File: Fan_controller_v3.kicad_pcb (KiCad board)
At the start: 4 copper layers, 50 x 25 mm, 0 parts

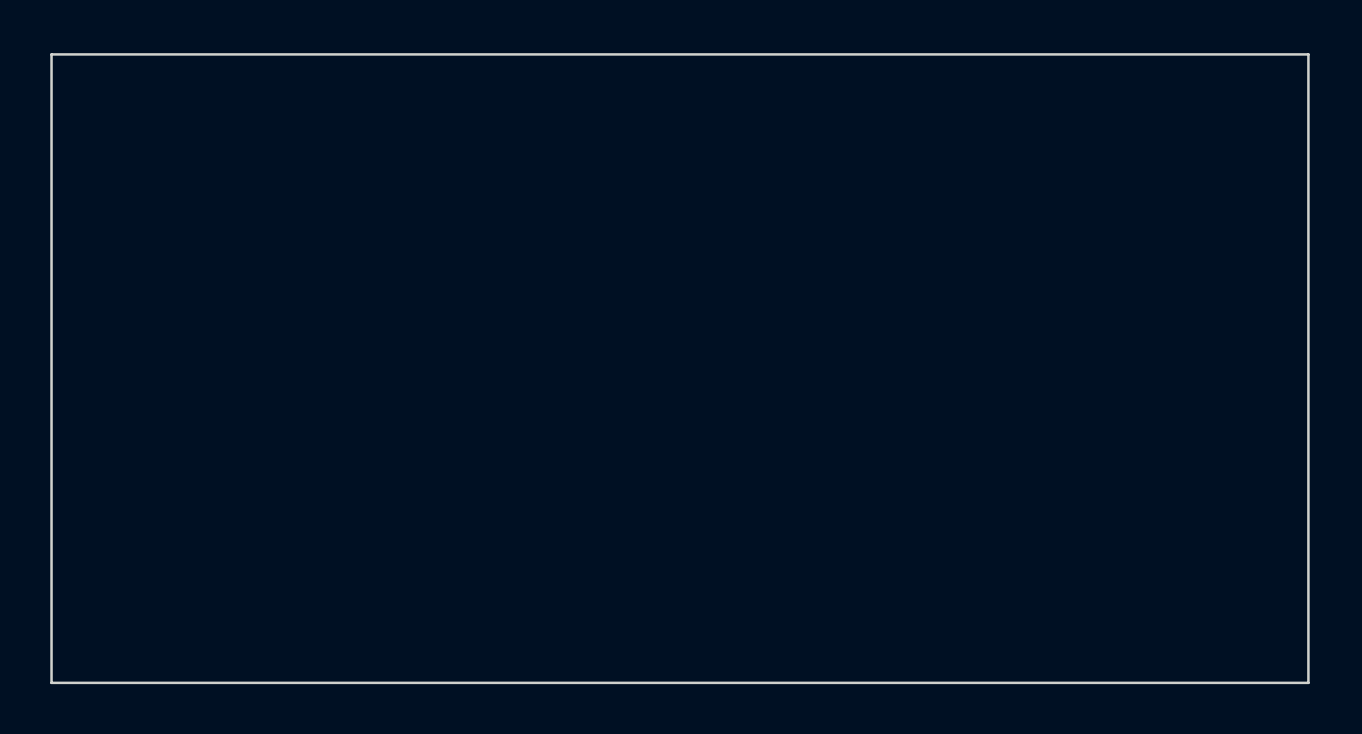
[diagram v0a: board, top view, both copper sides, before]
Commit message: Исправления в схеме и в печатной плате. Смещен вверх боковой конденсатор.
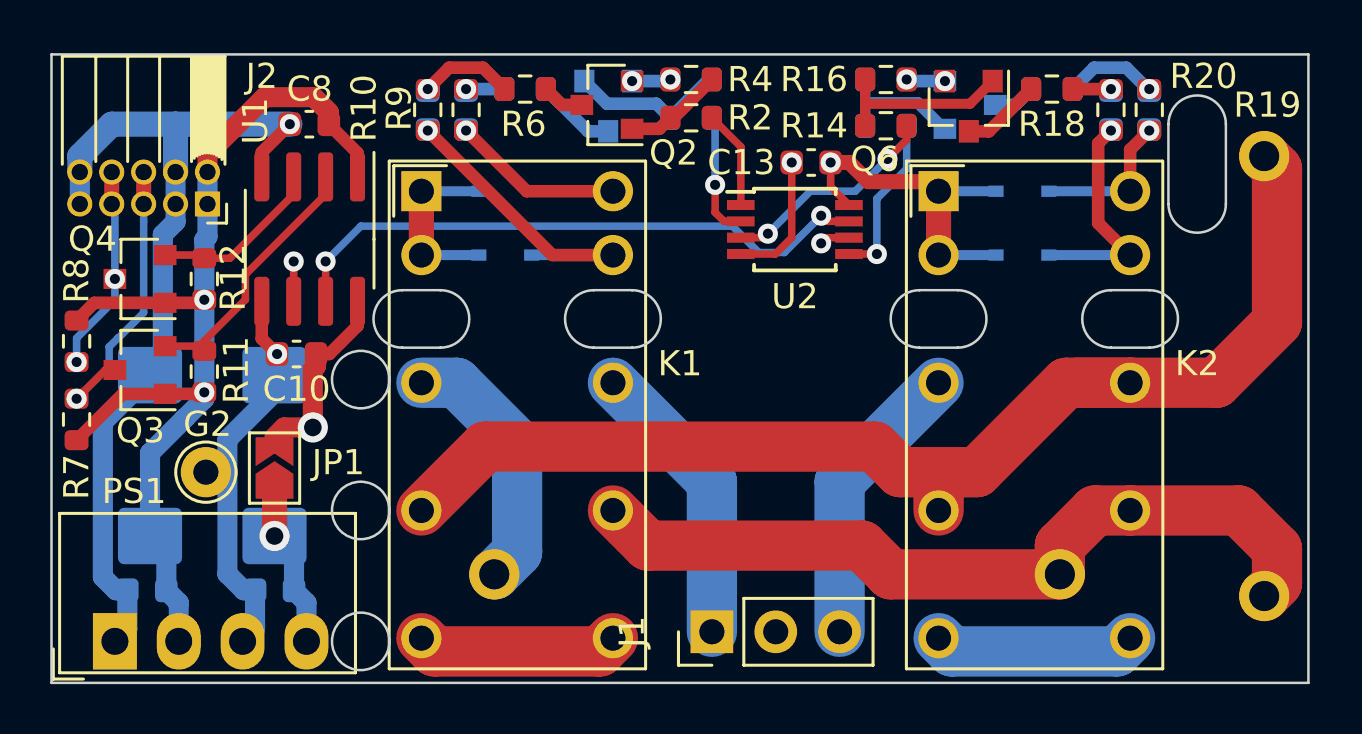
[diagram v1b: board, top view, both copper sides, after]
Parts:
- added C1: 10uF, Capacitor_Tantalum_SMD:CP_EIA-7343-43_Kemet-X_Pad2.25x2.55mm_HandSolder, B.Cu at (78.9, 91.0)
- added C10: 100nF, Capacitor_SMD:C_0603_1608Metric, F.Cu at (84.7, 86.9)
- added C11: 10uF, Capacitor_SMD:C_0603_1608Metric, B.Cu at (118.7, 77.2)
- added C12: 10uF, Capacitor_SMD:C_0603_1608Metric, B.Cu at (117.1, 77.2)
- added C13: 100nF, Capacitor_SMD:C_0603_1608Metric, F.Cu at (105.2, 79.3)
- added C2: 100nF, Capacitor_SMD:C_0603_1608Metric, B.Cu at (78.8, 96.3)
- added C3: 10uF, Capacitor_SMD:C_0603_1608Metric, B.Cu at (91.5, 77.2)
- added C4: 10uF, Capacitor_SMD:C_0603_1608Metric, B.Cu at (90.0, 77.2)
- added C5: 0.47uF, Modules:C_K73-17_W26.0mm_H15.0mm_T9.0mm_P22.5mm_d0.8mm_Horiz2, B.Cu at (92.6, 95.7)
- added C6: 100nF, Capacitor_SMD:C_0603_1608Metric, B.Cu at (83.9, 96.3)
- added C7: 0.22uF, Modules:C_K73-17_W20.0mm_H14.5mm_T8.0mm_P17.5mm_d0.8mm, B.Cu at (123.2, 79.0)
- added C8: 100nF, Capacitor_SMD:C_0603_1608Metric, F.Cu at (85.3, 77.8)
- added C9: 100uF, Capacitor_Tantalum_SMD:CP_EIA-7343-43_Kemet-X_Pad2.25x2.55mm_HandSolder, B.Cu at (83.9, 91.0)
- added D1: 1N4148WS, Diode_SMD:D_SOD-323, B.Cu at (93.0, 80.4)
- added D2: 1N4148WS, Diode_SMD:D_SOD-323, B.Cu at (93.0, 83.0)
- added D3: 1N4148WS, Diode_SMD:D_SOD-323, B.Cu at (113.6, 80.4)
- added D4: 1N4148WS, Diode_SMD:D_SOD-323, B.Cu at (113.6, 83.0)
- added G2: GND, TestPoint:TestPoint_THTPad_D2.0mm_Drill1.0mm, F.Cu at (81.1, 91.6)
- added J1: Load2, Modules:PinHeader_1x03_P2.54mm, F.Cu at (101.3, 98.0)
- added J2: Dig_mod_iface, Connector_PinSocket_1.27mm:PinSocket_2x05_P1.27mm_Horizontal, F.Cu at (81.2, 81.0)
- added JP1: 5P_en, Jumper:SolderJumper-2_P1.3mm_Open_TrianglePad1.0x1.5mm, F.Cu at (83.9, 91.5)
- added K1: HFD2_005-S-L2-D_Split, Modules:HFD2-005-S-L2-D, F.Cu at (89.7, 80.4)
- added K2: HFD2_005-S-L2-D_Split, Modules:HFD2-005-S-L2-D, F.Cu at (110.3, 80.4)
- added PS1: B0505S, Modules:B0505S, F.Cu at (77.5, 98.3)
- added Q1: 2N5551S, Package_TO_SOT_SMD:SOT-23, B.Cu at (97.1, 77.1)
- added Q2: 2N5551S, Package_TO_SOT_SMD:SOT-23, F.Cu at (97.1, 77.0)
- added Q3: BSS138, Package_TO_SOT_SMD:SOT-23, F.Cu at (78.5, 87.6)
- added Q4: BSS138, Package_TO_SOT_SMD:SOT-23, F.Cu at (78.5, 83.9)
- added Q5: 2N5551S, Package_TO_SOT_SMD:SOT-23, B.Cu at (111.5, 77.0)
- added Q6: 2N5551S, Package_TO_SOT_SMD:SOT-23, F.Cu at (111.5, 77.1)
- added R1: 1k, Resistor_SMD:R_0603_1608Metric, B.Cu at (100.4, 77.5)
- added R10: 820, Resistor_SMD:R_0603_1608Metric, F.Cu at (90.0, 77.2)
- added R11: 10k, Resistor_SMD:R_0603_1608Metric, F.Cu at (81.1, 87.6)
- added R12: 10k, Resistor_SMD:R_0603_1608Metric, F.Cu at (81.1, 83.9)
- added R13: 1k, Resistor_SMD:R_0603_1608Metric, B.Cu at (108.2, 77.8)
- added R14: 1k, Resistor_SMD:R_0603_1608Metric, F.Cu at (108.2, 77.8)
- added R15: 20k, Resistor_SMD:R_0603_1608Metric, B.Cu at (108.2, 76.0)
- added R16: 20k, Resistor_SMD:R_0603_1608Metric, F.Cu at (108.2, 76.0)
- added R17: 47, Resistor_SMD:R_0603_1608Metric, B.Cu at (114.8, 76.4)
- added R18: 47, Resistor_SMD:R_0603_1608Metric, F.Cu at (114.8, 76.4)
- added R19: 820, Resistor_SMD:R_0603_1608Metric, F.Cu at (118.7, 77.2)
- added R2: 1k, Resistor_SMD:R_0603_1608Metric, F.Cu at (100.4, 77.5)
- added R20: 820, Resistor_SMD:R_0603_1608Metric, F.Cu at (117.1, 77.2)
- added R3: 20k, Resistor_SMD:R_0603_1608Metric, B.Cu at (100.4, 76.0)
- added R4: 20k, Resistor_SMD:R_0603_1608Metric, F.Cu at (100.4, 76.0)
- added R5: 47, Resistor_SMD:R_0603_1608Metric, B.Cu at (93.8, 76.4)
- added R6: 47, Resistor_SMD:R_0603_1608Metric, F.Cu at (93.8, 76.4)
- added R7: 10G, Resistor_SMD:R_0603_1608Metric, F.Cu at (76.0, 89.5)
- added R8: 10G, Resistor_SMD:R_0603_1608Metric, F.Cu at (76.0, 86.4)
- added R9: 820, Resistor_SMD:R_0603_1608Metric, F.Cu at (91.5, 77.2)
- added U1: ADuM1251ARZ, Package_SO:SOIC-8_3.9x4.9mm_P1.27mm, F.Cu at (85.3, 82.3)
- added U2: PCA9536DP, Package_SO:TSSOP-8_3x3mm_P0.65mm, F.Cu at (104.6, 82.0)
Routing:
- net Net-(C7-Pad1): track 0.00 -> 48.6 mm
- net +5P: track 0.00 -> 41.2 mm, vias 0 -> 2
- net GND1: track 0.00 -> 36.0 mm, vias 0 -> 1
- net Net-(C5-Pad2): track 0.00 -> 31.9 mm
- net +5VP: track 0.00 -> 29.2 mm, vias 0 -> 2
- net /I2C_SCL: track 0.00 -> 24.9 mm, vias 0 -> 2
- net GND2: track 0.00 -> 24.8 mm, vias 0 -> 6
- net /I2C_SDA: track 0.00 -> 24.1 mm, vias 0 -> 2
- net Net-(C4-Pad2): track 0.00 -> 12.7 mm, vias 0 -> 1
- net /sda0: track 0.00 -> 12.1 mm, vias 0 -> 1
- net Net-(J1-Pad3): track 0.00 -> 11.5 mm
- net Net-(J1-Pad1): track 0.00 -> 11.5 mm
- net Net-(Q5-Pad1): track 0.00 -> 10.9 mm
- net Net-(Q3-Pad2): track 0.00 -> 10.6 mm
- net Net-(C5-Pad1): track 0.00 -> 10.4 mm
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- added copper zone on In1.Cu, net +5VP
- added copper zone on In2.Cu, net GND2
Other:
- outline, holes or cut-outs redrawn

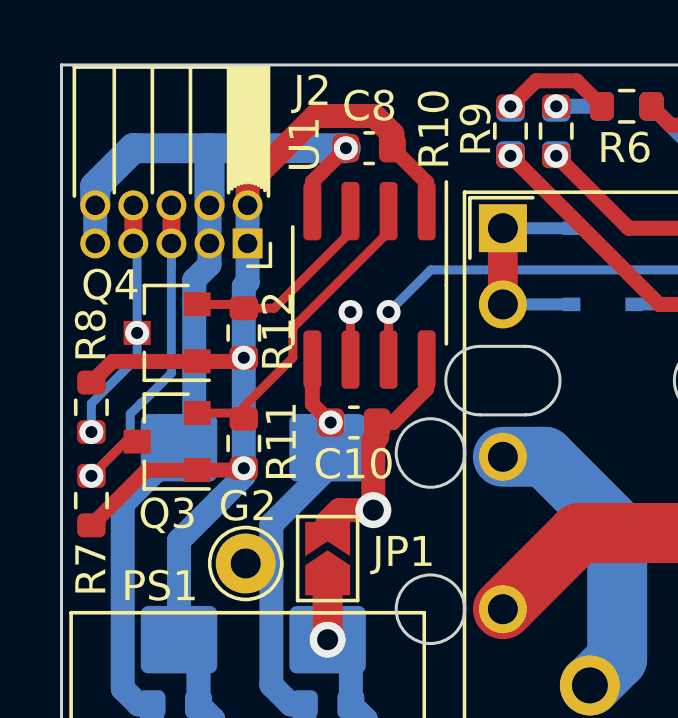
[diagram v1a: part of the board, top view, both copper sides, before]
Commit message: Добавлены недостающие компоненты схемы. Закончена трассировка платы.
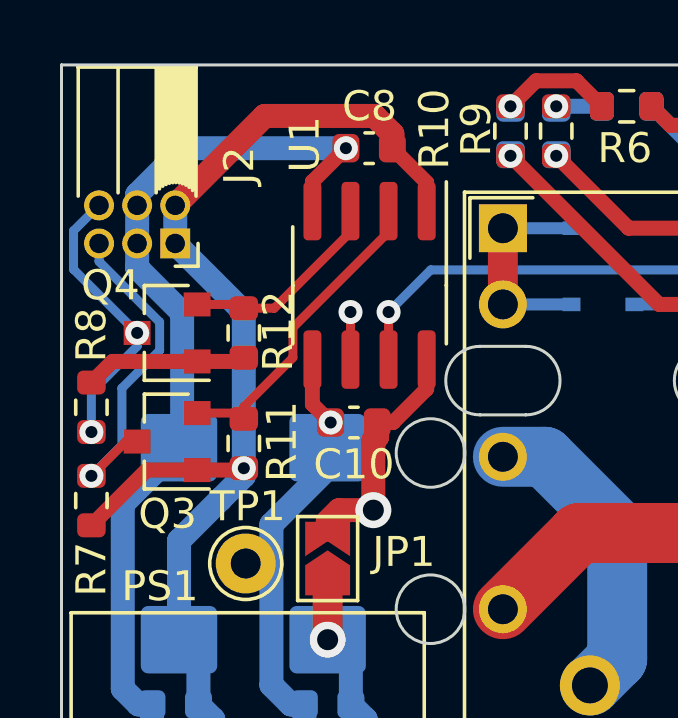
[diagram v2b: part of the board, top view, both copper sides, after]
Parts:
- J2: footprint Connector_PinSocket_1.27mm:PinSocket_2x05_P1.27mm_Horizontal -> Connector_PinSocket_1.27mm:PinSocket_2x03_P1.27mm_Horizontal
- moved J2 2.41 mm to (78.8, 81.0)
- renumbered G2 to TP1
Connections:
- J2 pad 6: /sda0 -> /scl0
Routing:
- net GND1: track 36.0 -> 31.7 mm
- net +5P: track 41.2 -> 44.0 mm, vias 2 -> 1
- net /scl0: track 8.24 -> 9.42 mm
- net /sda0: track 12.1 -> 11.5 mm
